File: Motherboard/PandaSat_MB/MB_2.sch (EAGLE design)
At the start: 164 parts, among them J1 503182-1852, J14 M023.5MM_LOCK, J15 M023.5MM_LOCK, J16 M023.5MM_LOCK, J2 10118194-0001LF, J3 DCJ0303, J4 BU-SMA-V, J5 BK-18650, K4 PE014006, Q1 IRLML2803, Q2 IRLML2803, Q3 IRLML2803, Q4 IRLML2803, Q5 MOSFET-PCHANNEL-SOIC8SOIC8, Q6 MOSFET-PCHANNEL-SOIC8SOIC8, Q7 MOSFET-PCHANNEL-SOIC8SOIC8, Q8 2N5088, U1 MAX706R, U10 DRV8848, U11 DRV8848, U2 LTC4121-4.2, U3 LSM9DS1, U4 MAX4372TEUK+T, U5 RFM23BP, U6 TPS54226PWPRPWP14_2P31X2P46-L, U7 ATSAMD51, U8 OKL-T3-W12

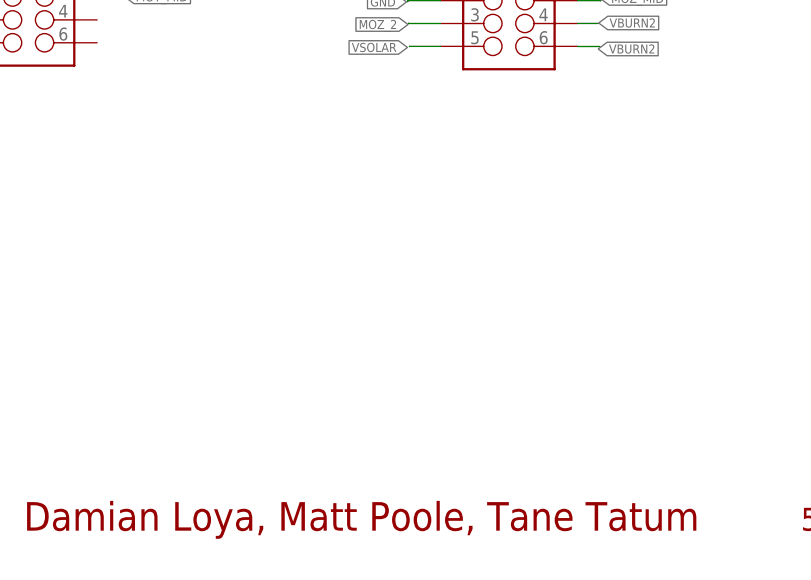
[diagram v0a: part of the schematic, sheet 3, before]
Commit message: Added USB Bypass
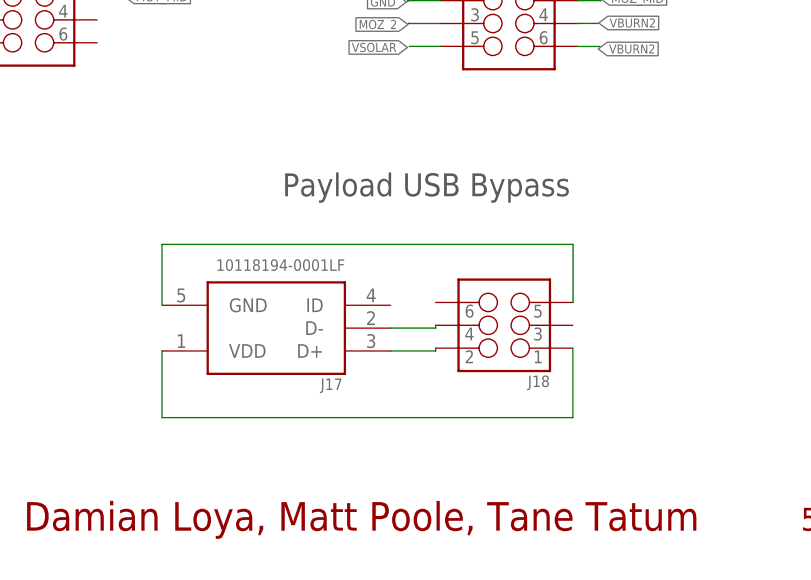
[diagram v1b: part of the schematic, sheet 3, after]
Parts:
- added J17: 10118194-0001LF, 10118194-0001LF:10118194-0001LF
- added J18: (no value), SparkFun-Connectors:M03X22X3_SILK_SM
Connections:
- new net N$22: J17.D+, J18.2
- new net N$40: J17.D-, J18.4
- new net N$42: J17.VDD, J18.1
- new net N$57: J17.GND, J18.5
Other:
- note added: "Payload USB Bypass"
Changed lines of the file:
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@@
 <part name="L2" library="pandasat" deviceset="CM322522" device="" value="10uH"/>
 <part name="L3" library="pandasat" deviceset="CM322522" device="" value="3.3uH"/>
+<part name="J17" library="10118194-0001LF" deviceset="10118194-0001LF" device=""/>
+<part name="J18" library="SparkFun-Connectors" deviceset="M03X2" device="2X3_SILK_SM"/>
 </parts>
 <sheets>
@@
 <text x="101.6" y="132.334" size="1.778" layer="97">Batteries in 2s2p config</text>
 <text x="87.152" y="53.32" size="2.54" layer="97" align="top-left">Test Points</text>
+<text x="183.692" y="47.32" size="2.54" layer="97" align="top-left">Payload USB Bypass</text>
 </plain>
 <instances>
@@
 </instance>
 <instance part="D1" gate="G$1" x="206.63" y="152.28" smashed="yes" rot="R270"/>
+<instance part="J17" gate="G$1" x="183.014" y="30.126" smashed="yes" rot="R180">
+<attribute name="NAME" x="190.395259375" y="24.52641875" size="1.27263125" layer="95" rot="R180"/>
+<attribute name="VALUE" x="190.65081875" y="37.76281875" size="1.272809375" layer="96" rot="R180"/>
+</instance>
+<instance part="J18" gate="G$1" x="208.342" y="30.438" smashed="yes" rot="R180">
+<attribute name="NAME" x="213.422" y="24.85" size="1.27" layer="95" rot="R180"/>
+<attribute name="VALUE" x="213.422" y="37.55" size="1.27" layer="96" rot="R180"/>
+</instance>
 </instances>
 <busses>
@@
 </segment>
 </net>
+<net name="N$22" class="0">
+<segment>
+<pinref part="J17" gate="G$1" pin="D+"/>
+<pinref part="J18" gate="G$1" pin="2"/>
+<wire x1="195.714" y1="27.586" x2="200.722" y2="27.586" width="0.1524" layer="91"/>
+<wire x1="200.722" y1="27.586" x2="200.722" y2="27.898" width="0.1524" layer="91"/>
+</segment>
+</net>
+<net name="N$40" class="0">
+<segment>
+<pinref part="J17" gate="G$1" pin="D-"/>
+<pinref part="J18" gate="G$1" pin="4"/>
+<wire x1="195.714" y1="30.126" x2="200.722" y2="30.126" width="0.1524" layer="91"/>
+<wire x1="200.722" y1="30.126" x2="200.722" y2="30.438" width="0.1524" layer="91"/>
+</segment>
+</net>
+<net name="N$42" class="0">
+<segment>
+<pinref part="J17" gate="G$1" pin="VDD"/>
+<wire x1="170.314" y1="27.586" x2="170.314" y2="20.18" width="0.1524" layer="91"/>
+<wire x1="170.314" y1="20.18" x2="215.962" y2="20.18" width="0.1524" layer="91"/>
+<pinref part="J18" gate="G$1" pin="1"/>
+<wire x1="215.962" y1="20.18" x2="215.962" y2="27.898" width="0.1524" layer="91"/>
+</segment>
+</net>
+<net name="N$57" class="0">
+<segment>
+<pinref part="J17" gate="G$1" pin="GND"/>
+<wire x1="170.314" y1="32.666" x2="170.314" y2="39.43" width="0.1524" layer="91"/>
+<wire x1="170.314" y1="39.43" x2="215.99" y2="39.43" width="0.1524" layer="91"/>
+<pinref part="J18" gate="G$1" pin="5"/>
+<wire x1="215.99" y1="39.43" x2="215.99" y2="32.978" width="0.1524" layer="91"/>
+<wire x1="215.99" y1="32.978" x2="215.962" y2="32.978" width="0.1524" layer="91"/>
+</segment>
+</net>

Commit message: Switched Barrel Jack to smd Changed Footprints for 2x3 conn to include casing Changed Hbridges to pair x&z instead of x&y fixed mislabeled net PL_PWR_EN -> PL_PWR_ENAB
Did all the signal routing, just need 5V and 3.3V
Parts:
- J10, J11, J12, J13, J18, J6, J7, J8, J9: device SparkFun-Connectors:M03X22X3_SILK_SM -> pandasat:CONN_03X22X3_SILK_MALE_PTH
- J3: value DCJ0303 -> PJ-036AH-SMT-TRSMD; device maholli:DCJ0303 -> pandasat:PJ-036AH-SMT-TRSMD
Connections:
- net DXY_FAULT renamed DXZ_FAULT
- net DZ_FAULT renamed DY_FAULT
- net MXY_EN renamed MXZ_EN
- net MZ_EN renamed MY_EN
- removed net N$57: J17.GND, J18.5
- removed net PL_PWR_EN: U7.PB01
- new net N$30: J17.D-, J18.3
- new net N$63: J7.6
- new net N$64: J7.4
- new net N$65: J8.6
- new net N$66: J8.4
- new net N$67: J9.6
- new net N$68: J9.4
- net MINY_1: now also U11.AIN1; no longer U10.BIN1
- net MINY_2: now also U11.AIN2; no longer U10.BIN2
- net MINZ_1: now also U10.BIN1; no longer U11.AIN1
- net MINZ_2: now also U10.BIN2; no longer U11.AIN2
- net MOY_1: now also U11.AOUT1; no longer U10.BOUT1
- net MOY_2: now also U11.AOUT2; no longer U10.BOUT2
- net MOZ_1: now also U10.BOUT1; no longer U11.AOUT1
- net MOZ_2: now also U10.BOUT2; no longer U11.AOUT2
- net N$22: now also J18.5; no longer J18.2
- net N$40: now also J17.VDD, J18.6; no longer J17.D-, J18.4
- net N$42: now also J17.GND, J18.2; no longer J17.VDD, J18.1
- net PL_PWR_ENAB: now also U7.PB01
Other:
- moved on the sheet: J3

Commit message: Updated schematic and MB as per meeting
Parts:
- removed F1: 500mA, SparkFun-PowerIC:PTCSMD
- removed JP1, JP2, JP3, JP4: JUMPER-PAD-3-2OF3_NC_BY_TRACE_SMALL, SparkFun-Passives:JUMPER-PAD-3-2OF3_NC_BY_TRACE_SMALL
- removed R36: 10k, resistor:R-US_R0603
- removed TP8, TP9: (no value), microbuilder:TESTPOINTROUND1MM
- removed U9: (no value), microbuilder:SPIFLASH_SOIC8
- added JP10: (no value), jumper:JP1E
- added R38: 665K, resistor:R-US_R0603
- added R39: 330K, resistor:R-US_R0603
- added U12: MR25H40MDF, maholli:MR25H40MDF
- J3: value PJ-036AH-SMT-TRSMD -> USBC; device pandasat:PJ-036AH-SMT-TRSMD -> pandasat:USBC
- LED1, LED2, LED3, LED4, LED5, LED6: device led:LEDCHIPLED-0603-TTW -> adafruit:LEDCHIP-LED0603
- R28, R29, R30, R31: value 62 -> 330
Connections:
- removed net 5V2: C11.1, D2.2, F1.2
- removed net A5: U7.PA06
- removed net I2C_SDOA/G: JP2.2, U3.SDO_A/G
- removed net N$21 (its old number): JP1.2, U3.SDO_M
- removed net N$23: JP3.2, U3.CS_M
- removed net N$26: JP4.2, U3.CS_A/G
- removed net N$32: D1.2, J3.1
- removed net N$42: J17.GND, J18.2
- removed net QSPI_CS: R36.2, U7.PB11, U9.SSEL
- removed net QSPI_DATA[0]: TP9.P$1, U7.PA08, U9.MOSI
- removed net QSPI_DATA[1]: U7.PA09, U9.MISO
- removed net QSPI_DATA[2]: U7.PA10, U9.#WP/IO2
- removed net QSPI_DATA[3]: U7.PA11, U9.#HOLD/IO3
- removed net QSPI_SCK: TP8.P$1, U7.PB10, U9.SCK
- new net A_VLEV: R38.1, R39.2, U7.PA05
- new net N$60: JP10.1, LED1.A, LED2.A, LED3.A, LED4.A
- new net SPI_CS_MRAM: U12.!CS, U7.PB11
- new net V_CH: D1.2, J3.VBUS, J3.VBUS2, J3.VBUS3, J3.VBUS4
- net 3.3V: now also JP10.2, U12.VDD, U3.CS_A/G, U3.CS_M, U3.SDO_A/G, U3.SDO_M; no longer JP1.3, JP2.3, JP3.3, JP4.3, R36.1, U9.VCC
- net GND: now also J17.GND, J18.1, J18.2, J18.4, J3.GND, J3.GND1, J3.GND2, J3.GND4, J3.SHELL1, J3.SHELL2, J3.SHELL3, J3.SHELL4, R39.1, U12.EP; no longer JP1.1, JP2.1, JP3.1, JP4.1, R28.1, R29.1, R30.1, R31.1, U9.VSS
- net I_BATT: now also U7.PA06; no longer U7.PA05
- net LED1: now also R28.1, U7.PA09; no longer LED1.A, U7.PB03
- net LED2: now also R29.1, U7.PA10; no longer LED2.A, U7.PB04
- net LED3: now also R30.1, U7.PA11; no longer LED3.A, U7.PA14
- net LED4: now also R31.1, U7.PB10; no longer LED4.A, U7.PA15
- net N$20: now also C11.1, D2.2; no longer F1.1
- net N$59: no longer J3.2, J3.3
- net P_GOOD: now also U7.PA08; no longer U7.PA27
- net SPI_MISO: now also U12.SO
- net SPI_MOSI: now also U12.SI
- net SPI_SCK: now also U12.SCK
- net VBATT_IN: now also R38.2
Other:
- note added: "Green LEDS 0.7V drop <8mA"
- note added: "Payload USB Pass Through"
- note removed: "Green LEDS 1.8V drop ~25mA"
- note removed: "Payload USB Bypass"

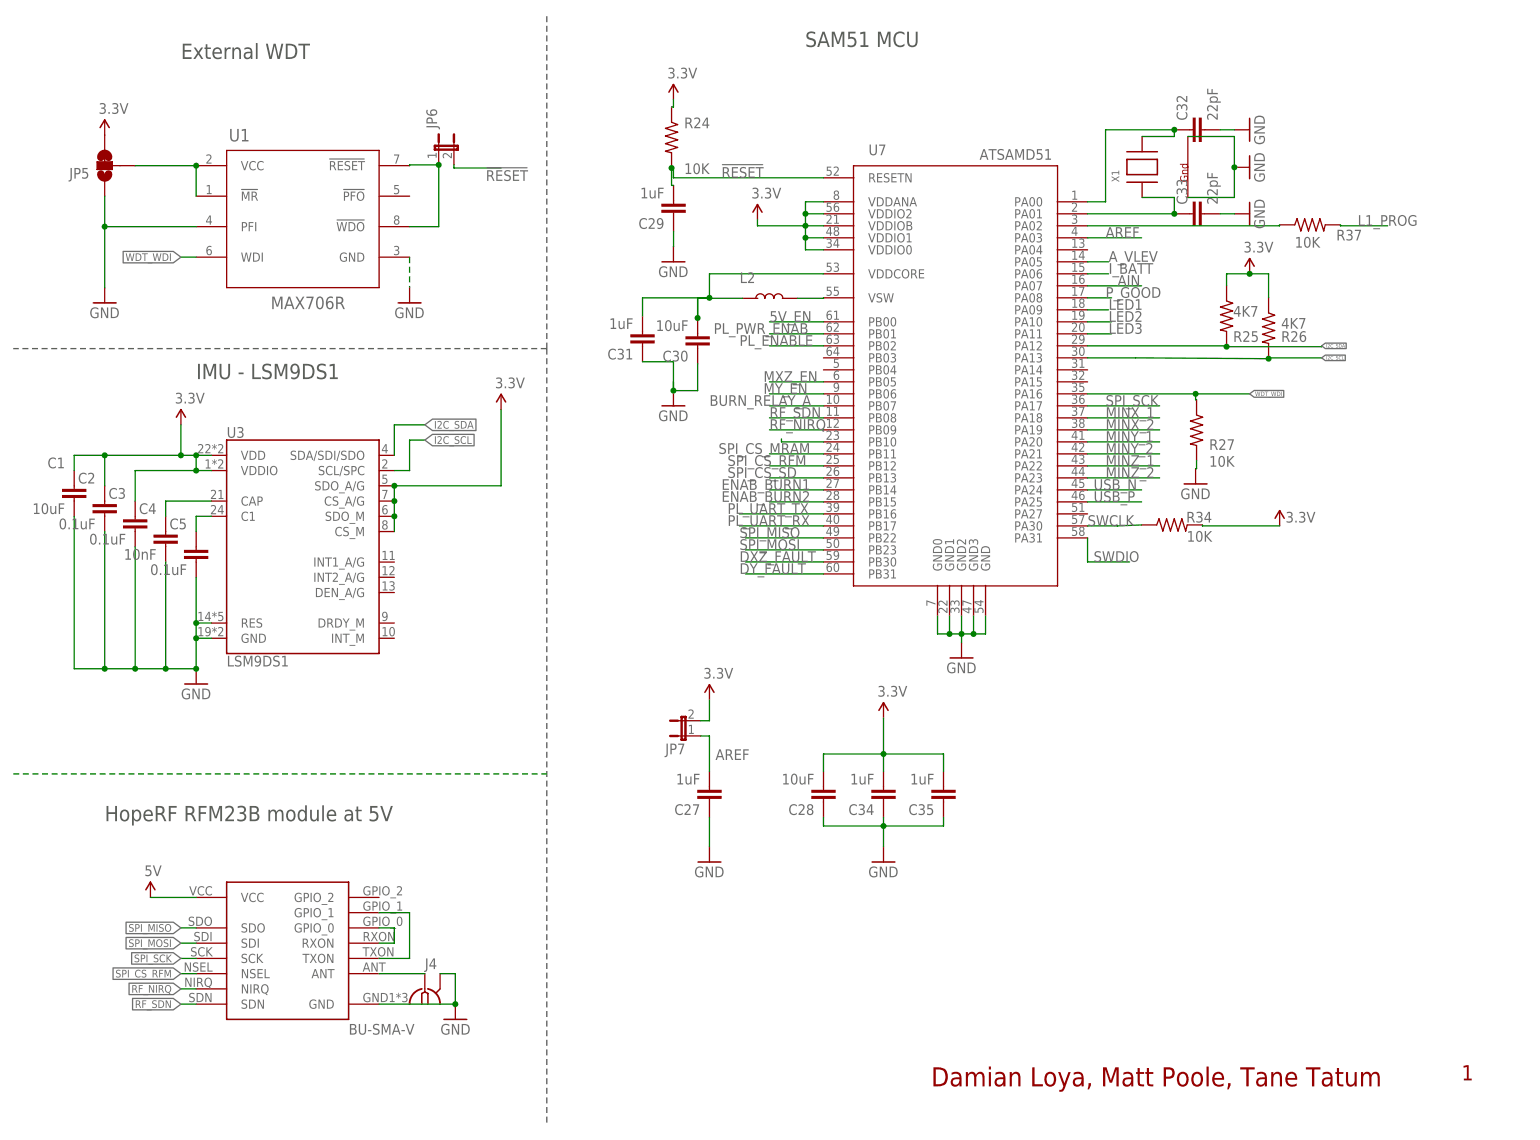
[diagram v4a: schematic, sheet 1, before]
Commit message: Re-added schematic frames
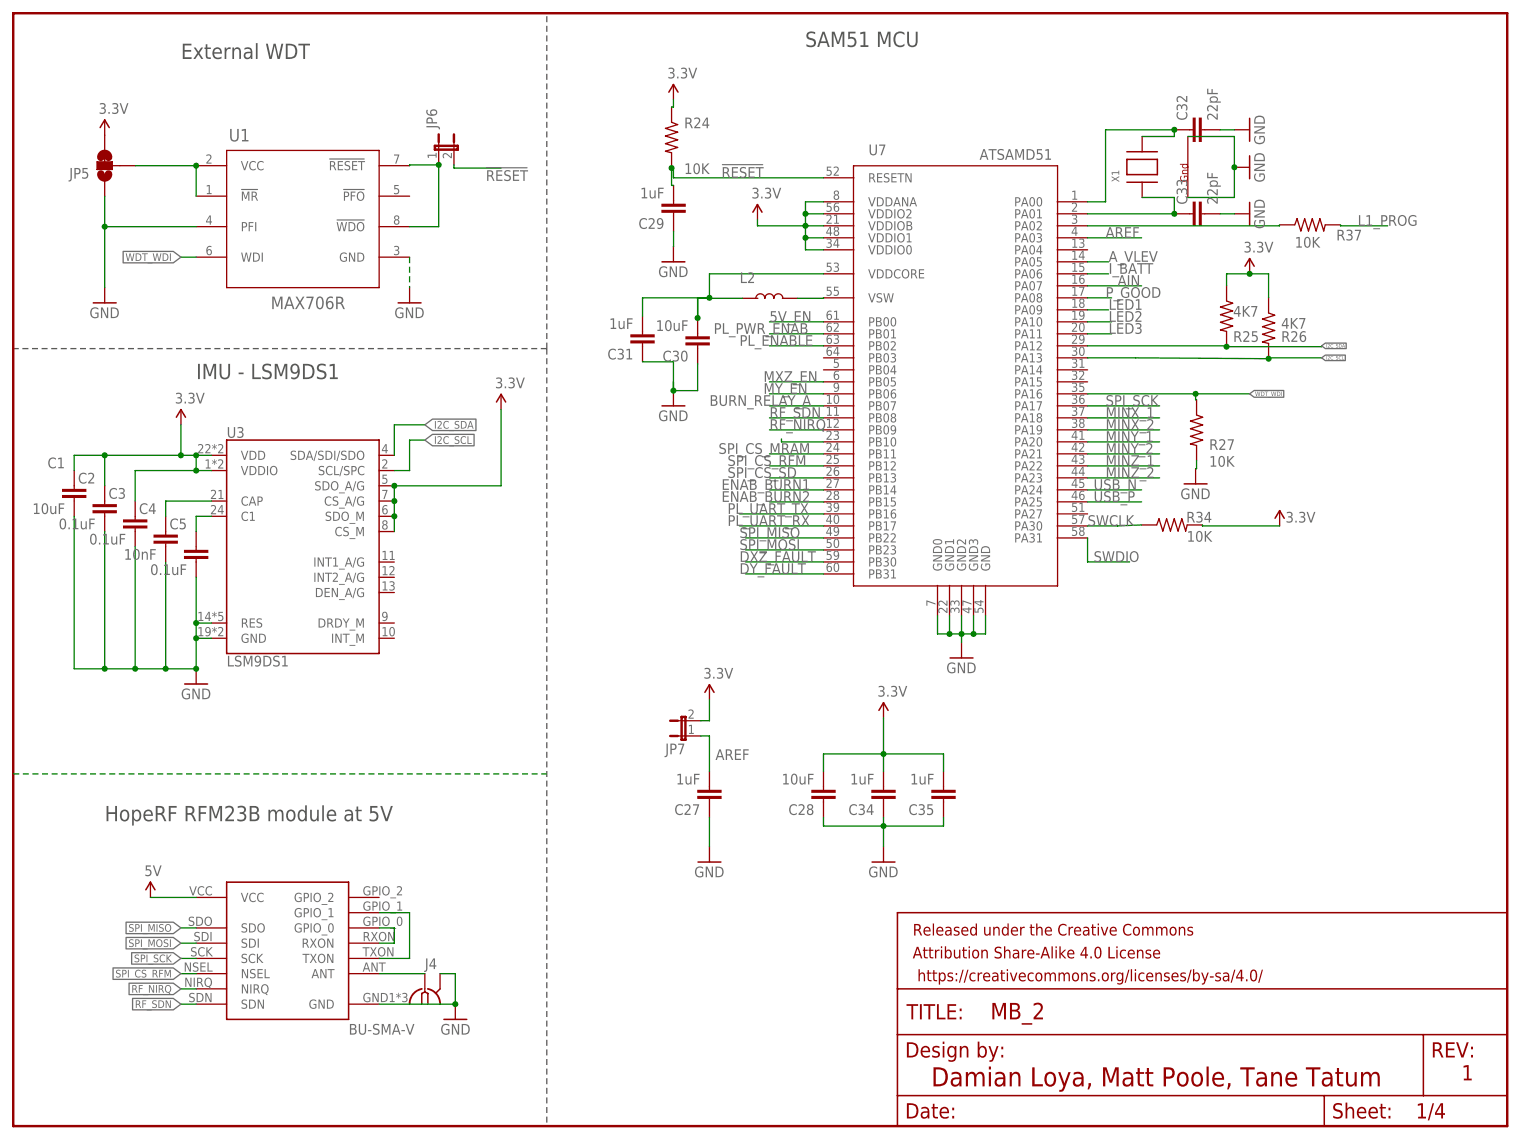
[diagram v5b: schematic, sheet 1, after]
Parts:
- added FRAME1, FRAME2, FRAME3, FRAME4: FRAME-LETTER, SparkFun-Aesthetics:FRAME-LETTER
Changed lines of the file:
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@@
 <?xml version="1.0" encoding="utf-8"?>
 <!DOCTYPE eagle SYSTEM "eagle.dtd">
-<eagle version="9.2.2">
+<eagle version="9.3.0">
 <drawing>
 <settings>
@@
 <part name="LED5" library="adafruit" deviceset="LED" device="CHIP-LED0603"/>
 <part name="LED6" library="adafruit" deviceset="LED" device="CHIP-LED0603"/>
+<part name="FRAME1" library="SparkFun-Aesthetics" deviceset="FRAME-LETTER" device=""/>
+<part name="FRAME2" library="SparkFun-Aesthetics" deviceset="FRAME-LETTER" device=""/>
+<part name="FRAME3" library="SparkFun-Aesthetics" deviceset="FRAME-LETTER" device=""/>
+<part name="FRAME4" library="SparkFun-Aesthetics" deviceset="FRAME-LETTER" device=""/>
 </parts>
 <sheets>
@@
 <attribute name="NAME" x="121.03" y="140.46" size="1.778" layer="95"/>
 </instance>
+<instance part="FRAME1" gate="G$1" x="0" y="0" smashed="yes"/>
+<instance part="FRAME1" gate="G$2" x="147.32" y="0" smashed="yes">
+<attribute name="LAST_DATE_TIME" x="160.02" y="1.27" size="2.54" layer="94" font="vector"/>
+<attribute name="SHEET" x="233.68" y="1.27" size="2.54" layer="94" font="vector"/>
+<attribute name="DRAWING_NAME" x="162.814" y="17.78" size="2.7432" layer="94" font="vector"/>
+</instance>
 </instances>
 <busses>
@@
 <attribute name="VALUE" x="239.715" y="154.428" size="1.778" layer="96" rot="R90"/>
 </instance>
+<instance part="FRAME2" gate="G$1" x="0" y="0" smashed="yes"/>
+<instance part="FRAME2" gate="G$2" x="147.32" y="0" smashed="yes">
+<attribute name="LAST_DATE_TIME" x="160.02" y="1.27" size="2.54" layer="94" font="vector"/>
+<attribute name="SHEET" x="233.68" y="1.27" size="2.54" layer="94" font="vector"/>
+<attribute name="DRAWING_NAME" x="162.814" y="17.78" size="2.7432" layer="94" font="vector"/>
+</instance>
 </instances>
 <busses>
@@
 <attribute name="VALUE" x="29.43" y="114.08" size="1.778" layer="96" align="center-left"/>
 </instance>
+<instance part="FRAME3" gate="G$1" x="0" y="0" smashed="yes"/>
+<instance part="FRAME3" gate="G$2" x="147.32" y="0" smashed="yes">
+<attribute name="LAST_DATE_TIME" x="160.02" y="1.27" size="2.54" layer="94" font="vector"/>
+<attribute name="SHEET" x="233.68" y="1.27" size="2.54" layer="94" font="vector"/>
+<attribute name="DRAWING_NAME" x="162.814" y="17.78" size="2.7432" layer="94" font="vector"/>
+</instance>
 </instances>
 <busses>
@@
 <attribute name="VALUE" x="181.86" y="127.84" size="1.778" layer="96"/>
 </instance>
+<instance part="FRAME4" gate="G$1" x="0" y="0" smashed="yes"/>
+<instance part="FRAME4" gate="G$2" x="147.32" y="0" smashed="yes">
+<attribute name="LAST_DATE_TIME" x="160.02" y="1.27" size="2.54" layer="94" font="vector"/>
+<attribute name="SHEET" x="233.68" y="1.27" size="2.54" layer="94" font="vector"/>
+<attribute name="DRAWING_NAME" x="162.814" y="17.78" size="2.7432" layer="94" font="vector"/>
+</instance>
 </instances>
